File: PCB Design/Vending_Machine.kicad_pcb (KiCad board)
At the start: 2 copper layers, 113.8 x 166.6 mm, 124 parts, among them J1 Mains, J11 Conn_I2C, J12 Conn_I2C, J2 Conn_0-7, J3 Conn_8, J31 Conn_01x15, J32 Conn_01x15, J33 UART0, J34 UART2, J35 GPIO, J36 Display, J37 I2C, J38 I2C, J39 SPI, J4 Conn_9, J40 GPIO, J7 Conn_Aux, J8 Conn_Sig, SW31 EN, SW32 BOOT, U1 AMS1117-3.3, U11 SX1509BIULTRT, U12 TCA9406DC, U31 AMS1117-3.3, U32 ESP32-WROOM-32UE, U33 TCA9406DC

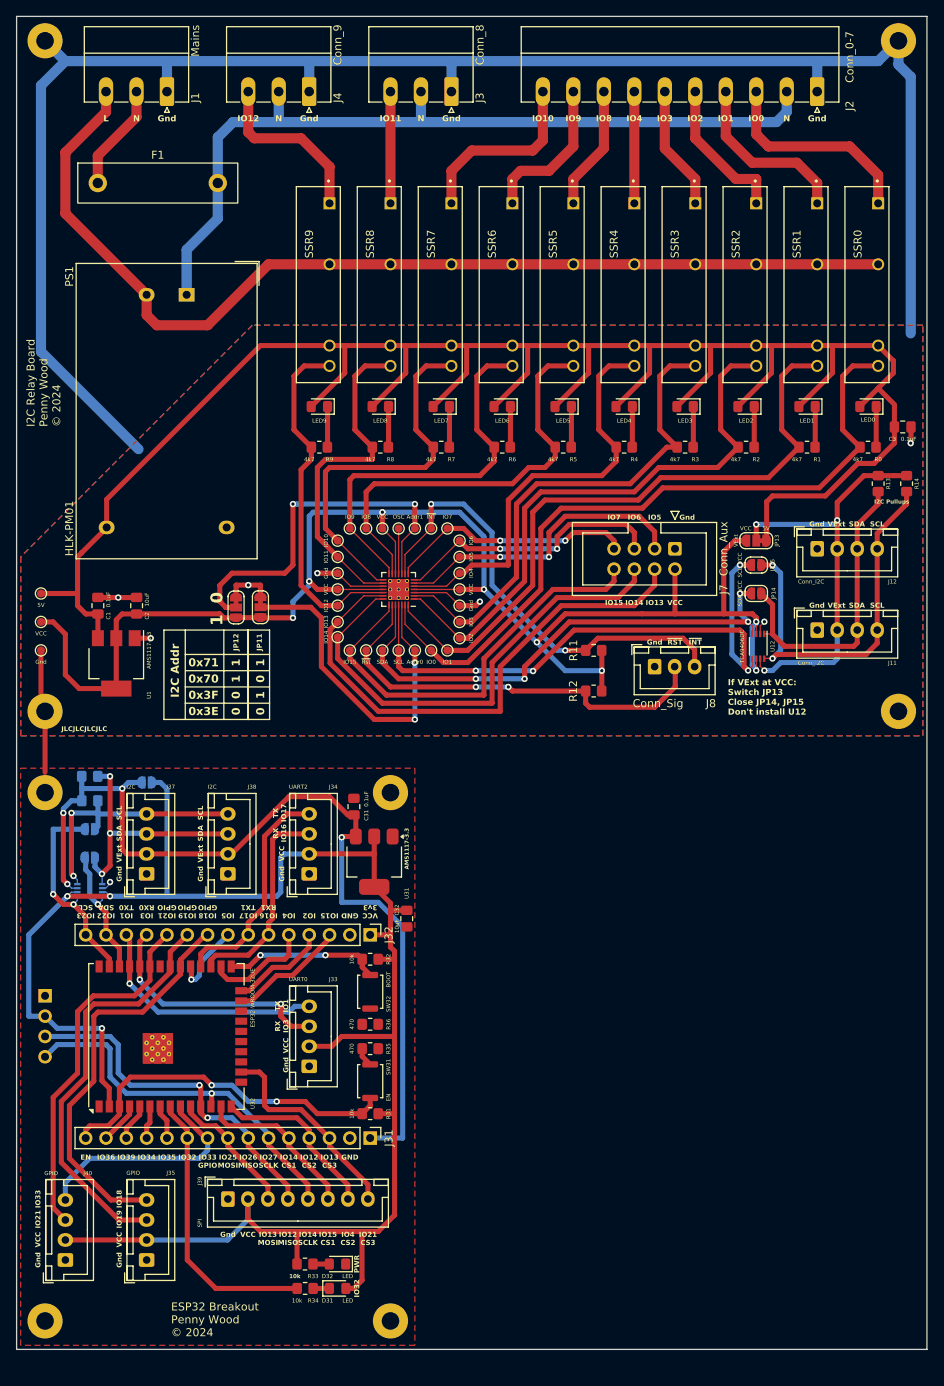
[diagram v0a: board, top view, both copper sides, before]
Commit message: Panelize
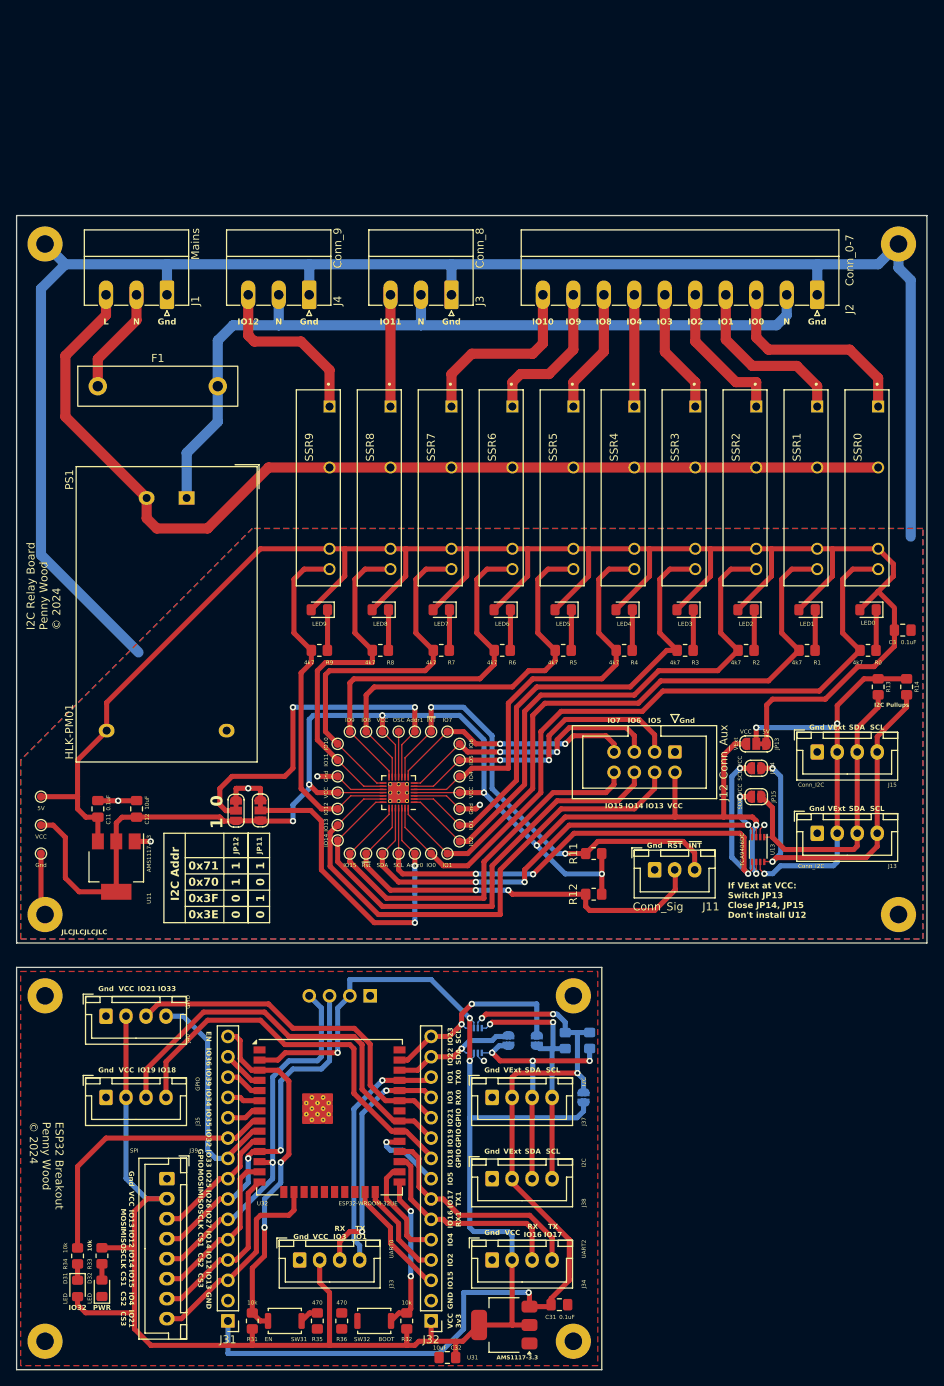
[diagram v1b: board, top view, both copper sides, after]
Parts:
- added B1: Relay, PCM_kikit:Board, F.Cu at (121.9, 138.2)
- added B2: Controller, PCM_kikit:Board, F.Cu at (120.4, 169.5)
- moved H32 72.3 mm to (116.8, 188.0), turned to -90 degrees
- moved H31 70.8 mm to (116.8, 144.8), turned to -90 degrees
- moved R37 70.7 mm to (118.9, 150.4), turned to -90 degrees
- moved C31 67.3 mm to (115.1, 183.4), turned to 0 degrees
- moved JP33 67.3 mm to (118.1, 157.5), turned to 90 degrees
- moved R38 66.6 mm to (115.8, 150.4), turned to -90 degrees
- moved JP31 61.8 mm to (112.3, 150.4), turned to -90 degrees
- moved U31 60.2 mm to (108.2, 185.9), turned to 180 degrees
- moved JP32 57.1 mm to (108.7, 150.4), turned to -90 degrees
- moved C32 55.1 mm to (101.1, 190.0), turned to 180 degrees
- moved J34 53.4 mm to (106.7, 177.8), turned to 0 degrees
- moved U33 51.8 mm to (104.6, 150.4), turned to 90 degrees
- moved J37 51.4 mm to (106.7, 157.5), turned to 0 degrees
- moved J38 50.4 mm to (106.7, 167.6), turned to 0 degrees
- moved J32 48.9 mm to (99.1, 185.4), turned to 180 degrees
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- renumbered C1 to C11, C2 to C12, J8 to J11, J7 to J12, J11 to J13, J12 to J15, JP15 to JP14, JP14 to JP15, U1 to U11, U11 to U12, U12 to U13
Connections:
- net +5V renamed /Relay Controller/+5V
- net LINE renamed /Relay Controller/Live
- net NEUT renamed /Relay Controller/Neut
- C11 pad 2: GND -> /Relay Controller/GND
- C12 pad 2: GND -> /Relay Controller/GND
- C3 pad 2: GND -> /Relay Controller/GND
- C31 pad 2: GND -> /Logic Controller/GND
- C32 pad 2: GND -> /Logic Controller/GND
- D32 pad 1: GND -> /Logic Controller/GND
- Gnd pad 17: GND -> /Relay Controller/GND
- Gnd pad : GND -> /Relay Controller/GND
- Gnd pad 3: GND -> /Relay Controller/GND
- H1 pad : GND -> /Relay Controller/GND
- H2 pad : GND -> /Relay Controller/GND
- H3 pad : GND -> /Relay Controller/GND
- H31 pad : GND -> /Logic Controller/GND
- H32 pad : GND -> /Logic Controller/GND
- H33 pad : GND -> /Logic Controller/GND
- H34 pad : GND -> /Logic Controller/GND
- H4 pad : GND -> /Relay Controller/GND
- J1 pad 1: GND -> /Relay Controller/GND
- J11 pad 1: GND -> /Relay Controller/GND
- J12 pad 1: GND -> /Relay Controller/GND
- J13 pad 1: GND -> /Relay Controller/GND
- J15 pad 1: GND -> /Relay Controller/GND
- J2 pad 1: GND -> /Relay Controller/GND
- J3 pad 1: GND -> /Relay Controller/GND
- J31 pad 2: GND -> /Logic Controller/GND
- J32 pad 2: GND -> /Logic Controller/GND
- J33 pad 1: GND -> /Logic Controller/GND
- J34 pad 1: GND -> /Logic Controller/GND
- J35 pad 1: GND -> /Logic Controller/GND
- J36 pad 1: GND -> /Logic Controller/GND
- J37 pad 1: GND -> /Logic Controller/GND
- J38 pad 1: GND -> /Logic Controller/GND
- J39 pad 1: GND -> /Logic Controller/GND
- J4 pad 1: GND -> /Relay Controller/GND
- J40 pad 1: GND -> /Logic Controller/GND
- JP11 pad 1: GND -> /Relay Controller/GND
- JP12 pad 1: GND -> /Relay Controller/GND
- PS1 pad 3: GND -> /Relay Controller/GND
- R35 pad 2: GND -> /Logic Controller/GND
- R36 pad 2: GND -> /Logic Controller/GND
- U11 pad 1: GND -> /Relay Controller/GND
- U12 pad 17: GND -> /Relay Controller/GND
- U12 pad 29: GND -> /Relay Controller/GND
- U12 pad 3: GND -> /Relay Controller/GND
- U13 pad 2: GND -> /Relay Controller/GND
- U31 pad 1: GND -> /Logic Controller/GND
- U32 pad 1: GND -> /Logic Controller/GND
- U32 pad 15: GND -> /Logic Controller/GND
- U32 pad 38: GND -> /Logic Controller/GND
- U32 pad 39: GND -> /Logic Controller/GND
- U33 pad 2: GND -> /Logic Controller/GND
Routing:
- net GND: track 267.2 -> 0.00 mm, vias 8 -> 0
- net /Relay Controller/GND: track 0.00 -> 256.1 mm, vias 0 -> 6
- net /Logic Controller/GND: track 0.00 -> 1.43 mm, vias 0 -> 1
- net /Logic Controller/IO4: track 13.9 -> 13.4 mm
- added copper zone on F.Cu, net /Logic Controller/GND
- added copper zone on B.Cu, net /Relay Controller/GND
- added copper zone on F.Cu, net /Relay Controller/GND
- removed copper zone on B.Cu, net GND
- removed copper zone on F.Cu, net GND
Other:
- board size 113.8 x 166.6 mm -> 113.8 x 144.3 mm
